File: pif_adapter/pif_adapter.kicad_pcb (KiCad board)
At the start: 2 copper layers, 11 x 22 mm, 11 parts, among them P1 Conn_02x20_Odd_Even, P10 Conn_01x01, P11 Conn_01x01, P2 PIF-NUS, P3 Conn_01x01, P4 Conn_01x01, P5 Conn_01x01, P6 Conn_01x01, P7 Conn_01x01, P8 Conn_01x01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

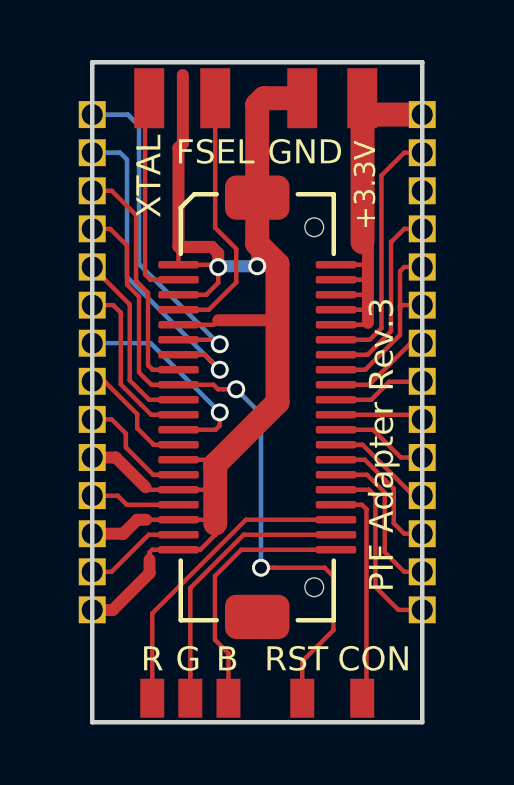
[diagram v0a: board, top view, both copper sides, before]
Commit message: changed connector to Hirose DF12
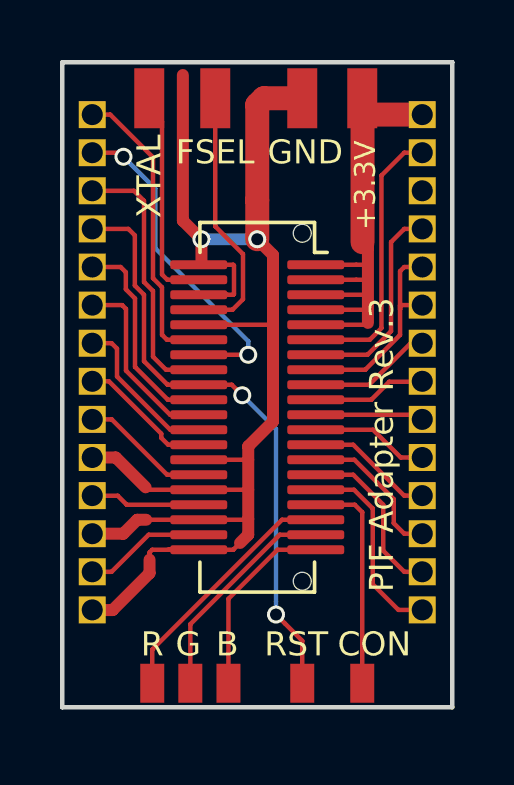
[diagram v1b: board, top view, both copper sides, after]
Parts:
- P1: footprint pif_adapter:Amphenol_MezzoStak-10106813_2x20x0.5mm -> pif_adapter:Hirose_DF12D-40DP-0.5V_2x20_P0.50mm_Vertical
- moved P10 0.50 mm to (150.0, 116.2)
- moved P11 0.50 mm to (148.0, 116.2)
- moved P7 0.50 mm to (143.0, 116.2)
- moved P8 0.50 mm to (144.3, 116.2)
- moved P9 0.50 mm to (145.5, 116.2)
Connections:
- P1 pad : GND -> (no net)
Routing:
- net /OUTPUT_RST: track 22.6 -> 20.0 mm
- net /BLUE: track 8.56 -> 6.40 mm
- net /GREEN: track 9.16 -> 7.38 mm
- net /RED: track 10.1 -> 8.37 mm
- net /NMI_CPU: track 6.98 -> 5.29 mm, vias 1 -> 0
- net /CLK_CIC_EEP: track 11.5 -> 9.95 mm, vias 1 -> 0
- net /CIC_DIO: track 6.29 -> 7.05 mm
- net /CON1: track 7.49 -> 6.73 mm
- net /CIC_DCLK: track 8.14 -> 8.89 mm
- net /RC_POR: track 11.0 -> 11.1 mm, vias 1 -> 2
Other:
- board size 11 x 22 mm -> 13 x 21.5 mm

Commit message: - updated revision info - cut edges through vias
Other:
- board size 13 x 21.5 mm -> 11 x 21.5 mm
- board text added: "PIF Adapter Rev.4"
- board text removed: "PIF Adapter Rev.3"
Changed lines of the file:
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@@
   )
   (page A4)
+  (title_block
+    (title "UltraPIF Adapter")
+    (date 2020-03-04)
+    (rev 4)
+  )
   (layers
     (0 F.Cu signal)
@@
     (arrow2b (pts (xy 155 95.5) (xy 155.586421 96.626504)))
   )
-  (gr_text "PIF Adapter Rev.3" (at 150.65 108.25 90) (layer F.SilkS)
+  (gr_text "PIF Adapter Rev.4" (at 150.65 108.25 90) (layer F.SilkS)
     (effects (font (size 0.8 0.8) (thickness 0.15)))
   )
@@
     (effects (font (size 0.8 0.8) (thickness 0.15)))
   )
-  (gr_line (start 153 117) (end 153 95.5) (layer Edge.Cuts) (width 0.15))
-  (gr_line (start 140 117) (end 153 117) (layer Edge.Cuts) (width 0.15))
+  (gr_line (start 152 117) (end 152 95.5) (layer Edge.Cuts) (width 0.15))
+  (gr_line (start 141 117) (end 152 117) (layer Edge.Cuts) (width 0.15))
   (dimension 21.5 (width 0.3) (layer Dwgs.User)
     (gr_text "21,500 mm" (at 136.9 106.25 270) (layer Dwgs.User)
@@
     (arrow2b (pts (xy 140 94) (xy 141.126504 93.413579)))
   )
-  (gr_line (start 140 95.5) (end 140 117) (layer Edge.Cuts) (width 0.15))
-  (gr_line (start 140 95.5) (end 153 95.5) (layer Edge.Cuts) (width 0.15))
+  (gr_line (start 141 95.5) (end 141 117) (layer Edge.Cuts) (width 0.15))
+  (gr_line (start 141 95.5) (end 152 95.5) (layer Edge.Cuts) (width 0.15))
   (segment (start 141.6 97.245) (end 141 97.245) (width 0.15) (layer F.Cu) (net 1))
   (segment (start 143.49 104.75) (end 143.325 104.585) (width 0.15) (layer F.Cu) (net 1))
